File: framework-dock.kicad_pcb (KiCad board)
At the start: 2 copper layers, 66 x 40 mm, 14 parts, among them P1 USB_C_Plug_USB2.0, P2 USB_C_Plug_USB2.0

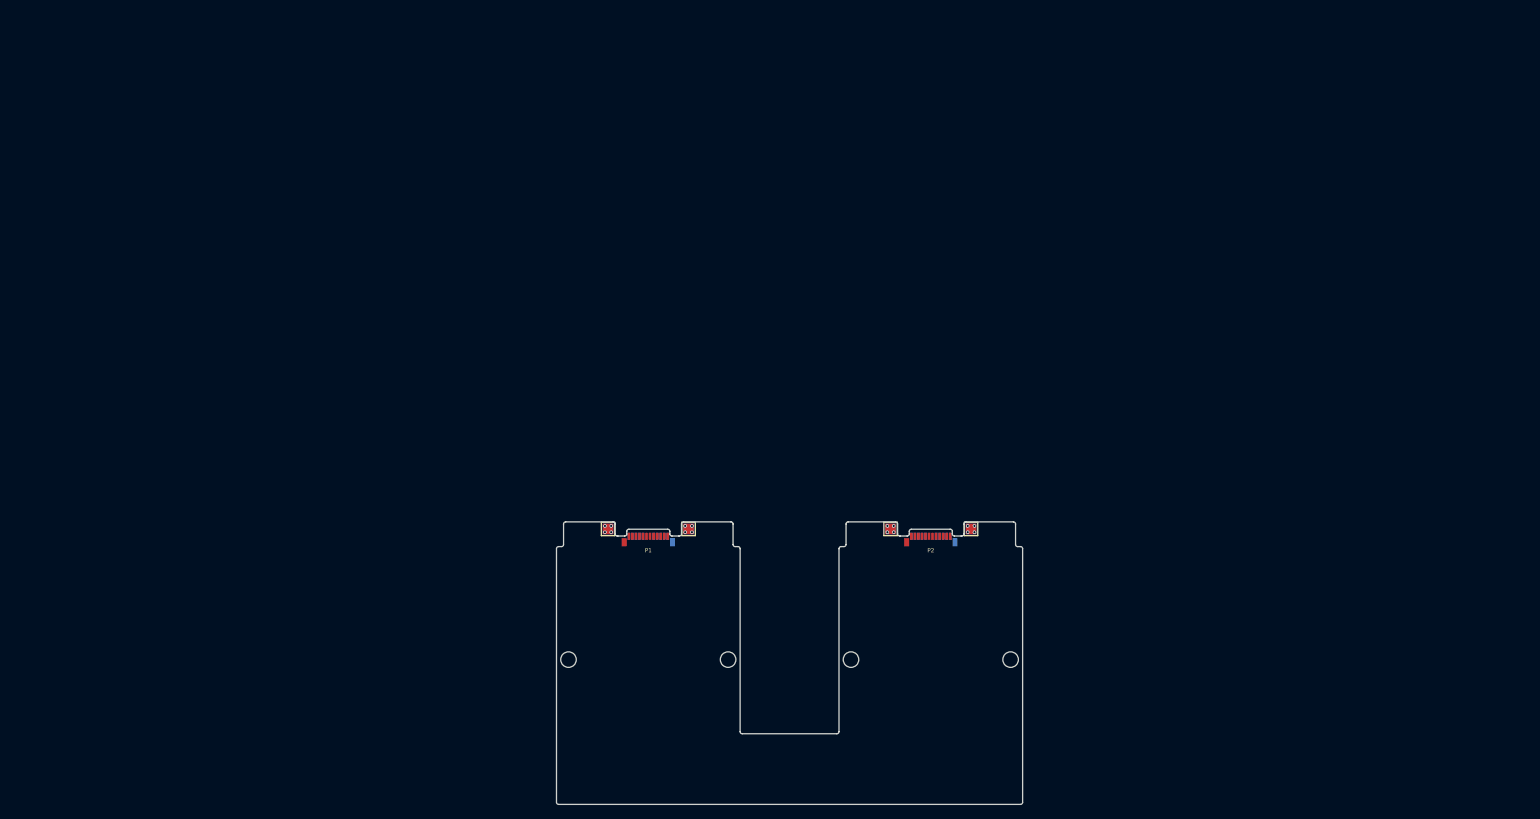
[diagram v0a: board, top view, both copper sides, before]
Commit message: Updated Basic PCB Outline
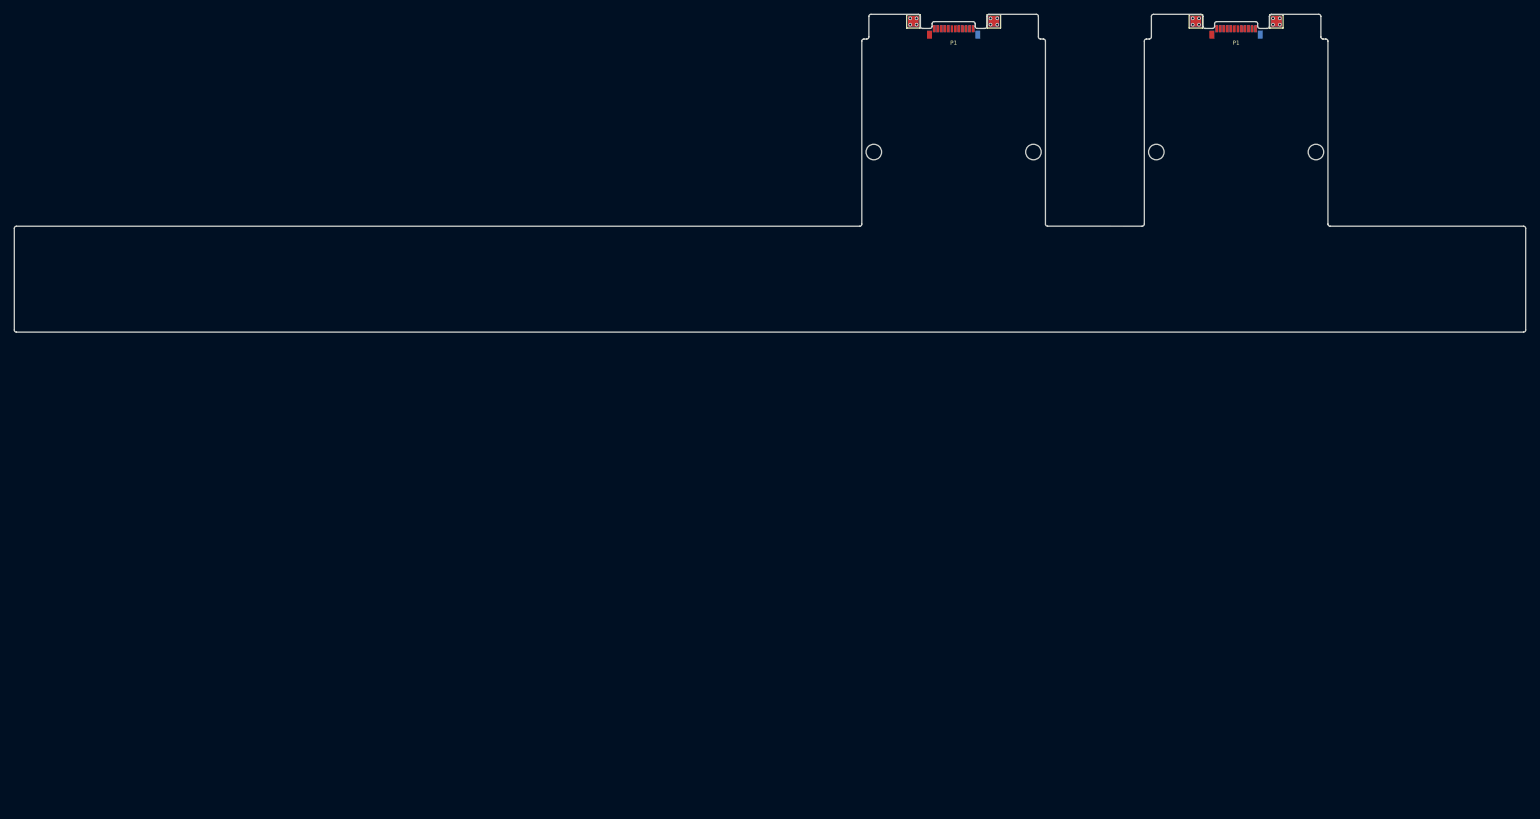
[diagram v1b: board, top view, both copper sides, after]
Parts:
- moved H1 83.9 mm to (171.9, 74.6)
- moved H1 83.9 mm to (211.9, 74.6)
- moved TP3 83.9 mm to (188.9, 56.1)
- moved TP3 83.9 mm to (228.9, 56.1)
- moved TP4 83.9 mm to (188.9, 56.1)
- moved TP4 83.9 mm to (228.9, 56.1)
- moved H2 83.9 mm to (194.5, 74.6)
- moved H2 83.9 mm to (234.5, 74.6)
- moved P1 83.9 mm to (183.2, 57.1)
- moved P1 83.9 mm to (223.2, 57.1)
- moved TP1 83.9 mm to (177.5, 56.1)
- moved TP1 83.9 mm to (217.5, 56.1)
- moved TP2 83.9 mm to (177.5, 56.1)
- moved TP2 83.9 mm to (217.5, 56.1)
- renumbered P2 to P1
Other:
- board size 66 x 40 mm -> 214 x 45 mm

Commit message: Updated Basic Board Outline
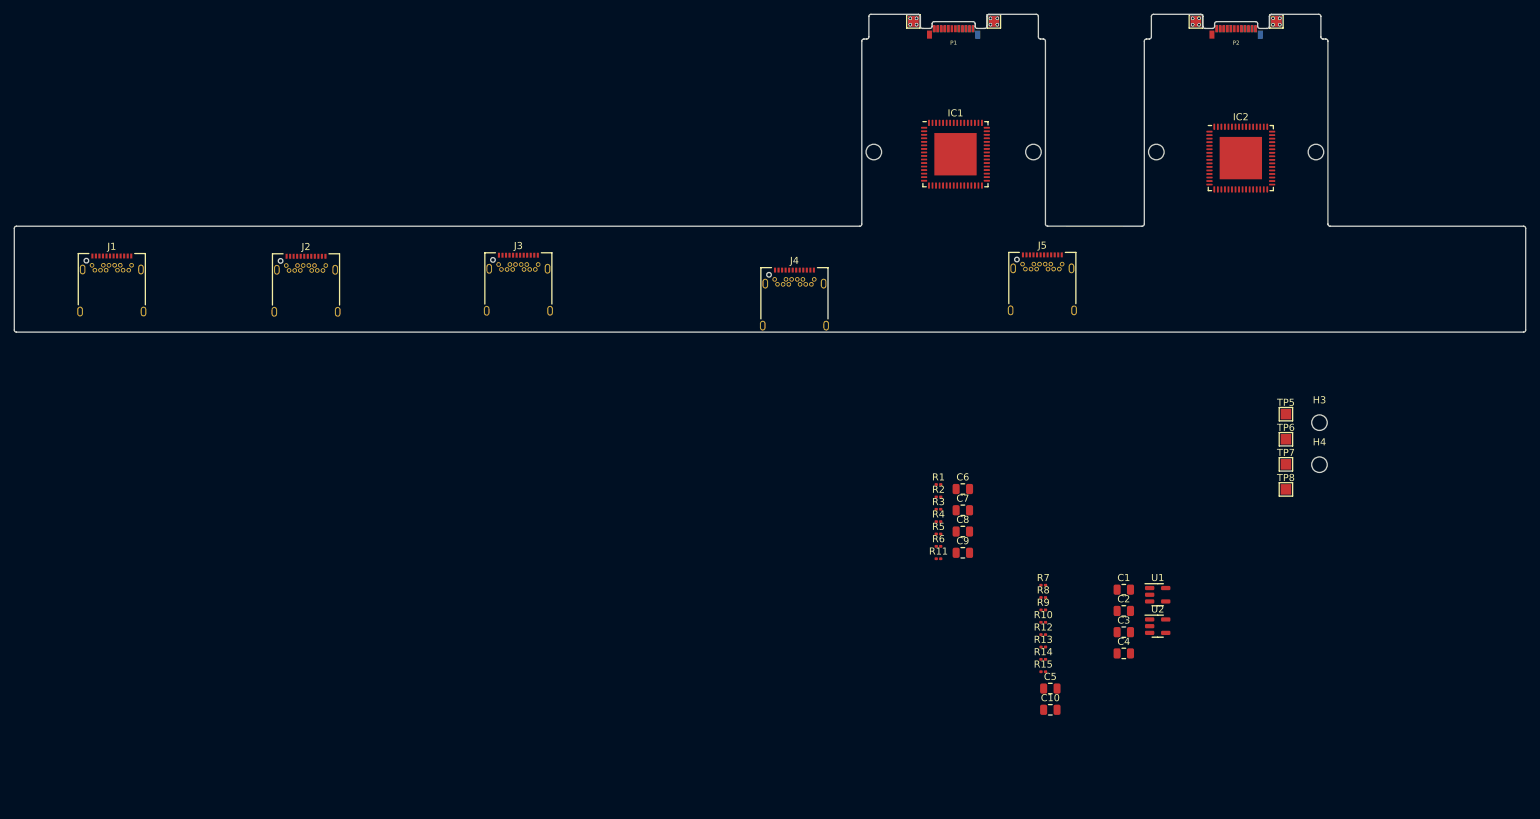
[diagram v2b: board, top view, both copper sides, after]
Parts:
- added C1: 10uF, Capacitor_SMD:C_0805_2012Metric, F.Cu at (207.3, 136.6)
- added C10: 10uF, Capacitor_SMD:C_0805_2012Metric, F.Cu at (196.9, 153.6)
- added C2: 10uF, Capacitor_SMD:C_0805_2012Metric, F.Cu at (207.3, 139.6)
- added C3: 10uF, Capacitor_SMD:C_0805_2012Metric, F.Cu at (207.3, 142.6)
- added C4: 10uF, Capacitor_SMD:C_0805_2012Metric, F.Cu at (207.3, 145.6)
- added C5: 10uF, Capacitor_SMD:C_0805_2012Metric, F.Cu at (196.9, 150.6)
- added C6: 0.1uF, Capacitor_SMD:C_0805_2012Metric, F.Cu at (184.5, 122.3)
- added C7: 0.1uF, Capacitor_SMD:C_0805_2012Metric, F.Cu at (184.5, 125.4)
- added C8: 0.1uF, Capacitor_SMD:C_0805_2012Metric, F.Cu at (184.5, 128.4)
- added C9: 0.1uF, Capacitor_SMD:C_0805_2012Metric, F.Cu at (184.5, 131.4)
- added H3: MountingHole, MountingHole:MountingHole_2.2mm_M2, F.Cu at (235.0, 113.0)
- added H4: MountingHole, MountingHole:MountingHole_2.2mm_M2, F.Cu at (235.0, 118.9)
- added IC1: TUSB8042ARGCT, Package_DFN_QFN:QFN-64-1EP_9x9mm_P0.5mm_EP6x6mm, F.Cu at (183.5, 74.9)
- added IC2: TUSB8042ARGCT, Package_DFN_QFN:QFN-64-1EP_9x9mm_P0.5mm_EP6x6mm, F.Cu at (223.9, 75.5)
- added J1: USB_C_Receptacle, Connector_USB:USB_C_Receptacle_Amphenol_12401548E4-2A, F.Cu at (64.0, 94.4)
- added J2: USB_C_Receptacle, Connector_USB:USB_C_Receptacle_Amphenol_12401548E4-2A, F.Cu at (91.5, 94.4)
- added J3: USB_C_Receptacle, Connector_USB:USB_C_Receptacle_Amphenol_12401548E4-2A, F.Cu at (121.6, 94.3)
- added J4: USB_C_Receptacle, Connector_USB:USB_C_Receptacle_Amphenol_12401548E4-2A, F.Cu at (160.7, 96.4)
- added J5: USB_C_Receptacle, Connector_USB:USB_C_Receptacle_Amphenol_12401548E4-2A, F.Cu at (195.8, 94.2)
- added R1: 5.1k, Resistor_SMD:R_0201_0603Metric, F.Cu at (181.1, 121.7)
- added R10: 4.7k, Resistor_SMD:R_0201_0603Metric, F.Cu at (195.9, 141.2)
- added R11: 5.1k, Resistor_SMD:R_0201_0603Metric, F.Cu at (181.1, 132.2)
- added R12: 4.7k, Resistor_SMD:R_0201_0603Metric, F.Cu at (195.9, 143.0)
- added R13: 4.7k, Resistor_SMD:R_0201_0603Metric, F.Cu at (195.9, 144.7)
- added R14: 10k, Resistor_SMD:R_0201_0603Metric, F.Cu at (195.9, 146.5)
- added R15: 90.9k, Resistor_SMD:R_0201_0603Metric, F.Cu at (195.9, 148.2)
- added R2: 5.1k, Resistor_SMD:R_0201_0603Metric, F.Cu at (181.1, 123.5)
- added R3: 5.1k, Resistor_SMD:R_0201_0603Metric, F.Cu at (181.1, 125.2)
- added R4: 5.1k, Resistor_SMD:R_0201_0603Metric, F.Cu at (181.1, 127.0)
- added R5: 5.1k, Resistor_SMD:R_0201_0603Metric, F.Cu at (181.1, 128.7)
- added R6: 5.1k, Resistor_SMD:R_0201_0603Metric, F.Cu at (181.1, 130.5)
- added R7: 90.9k, Resistor_SMD:R_0201_0603Metric, F.Cu at (195.9, 136.0)
- added R8: 10k, Resistor_SMD:R_0201_0603Metric, F.Cu at (195.9, 137.7)
- added R9: 4.7k, Resistor_SMD:R_0201_0603Metric, F.Cu at (195.9, 139.5)
- added TP5: TestPoint, TestPoint:TestPoint_Pad_1.5x1.5mm, F.Cu at (230.3, 111.8)
- added TP6: TestPoint, TestPoint:TestPoint_Pad_1.5x1.5mm, F.Cu at (230.3, 115.3)
- added TP7: TestPoint, TestPoint:TestPoint_Pad_1.5x1.5mm, F.Cu at (230.3, 118.8)
- added TP8: TestPoint, TestPoint:TestPoint_Pad_1.5x1.5mm, F.Cu at (230.3, 122.4)
- added U1: AP2112K-1.2, Package_TO_SOT_SMD:SOT-23-5, F.Cu at (212.1, 137.3)
- added U2: AP2112K-3.3, Package_TO_SOT_SMD:SOT-23-5, F.Cu at (212.1, 141.8)
- P1: value USB_C_Plug_USB2.0 -> USB_C_Plug
- P2: renamed from P1; value USB_C_Plug_USB2.0 -> USB_C_Plug
- renumbered H1 to H3, H2 to H4, TP1 to TP5, TP2 to TP6, TP3 to TP7, TP4 to TP8
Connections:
- P1 pad A2: (no net) -> TX1-
